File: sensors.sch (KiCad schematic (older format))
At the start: 1 part, among them U5 ICM-20948

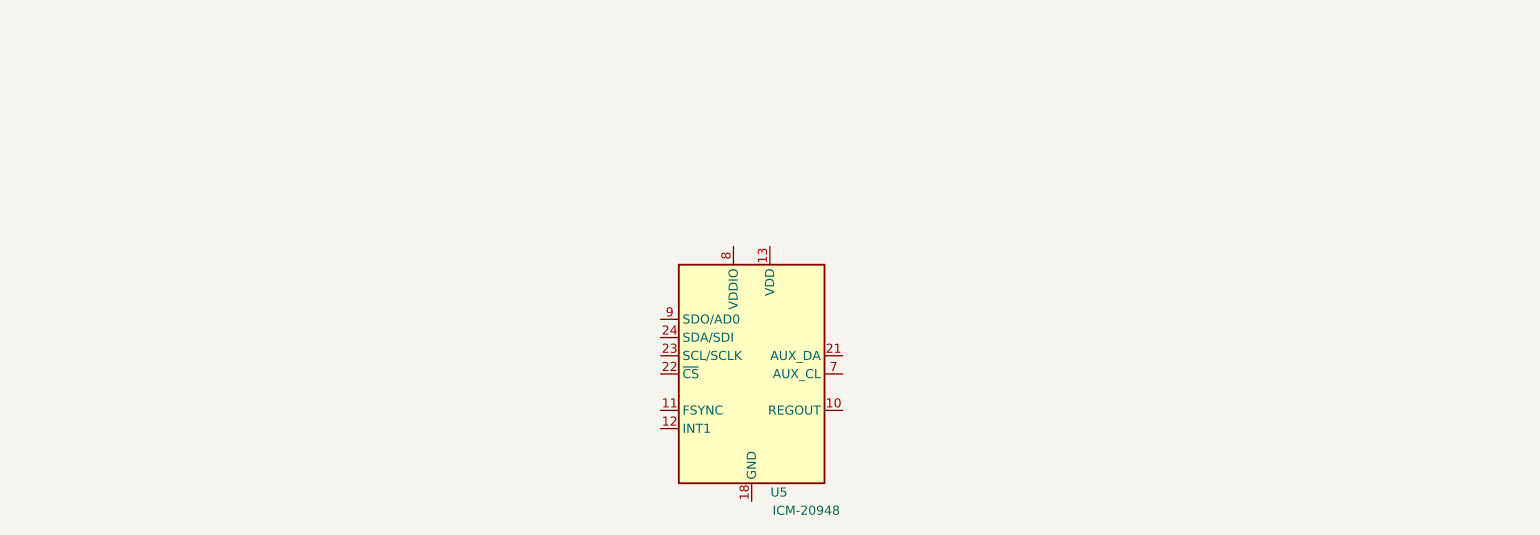
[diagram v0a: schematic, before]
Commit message: First full version of a schematic
This commit is a quicksave of completed but not reviewed schematic.
Added pressure sensor, finished IMU wiring, finished top-level
schematic, added pin header, placed LEDs and many others.
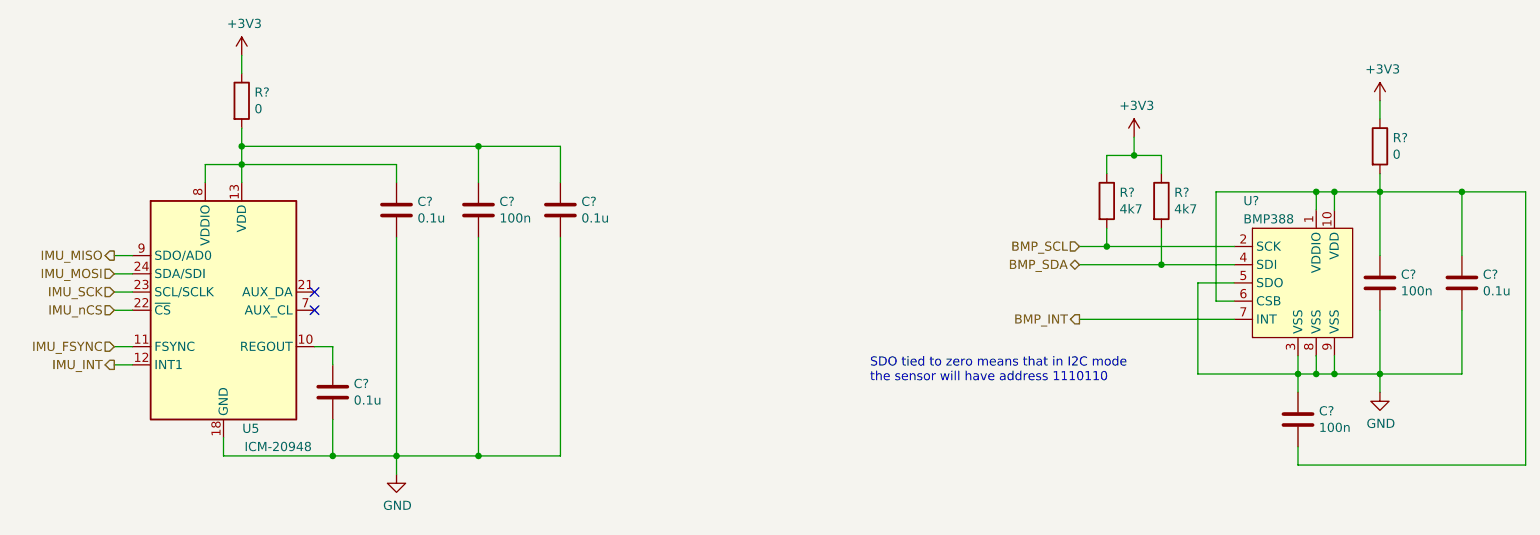
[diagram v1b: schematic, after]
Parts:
- added C? (x3): 100n, symbol Device:C
- added C? (x4): 0.1u, symbol Device:C
- added R? (x2): 4k7, symbol Device:R
- added R? (x2): 0, symbol Device:R
- added U?: BMP388, himudev:Bosch_LGA-10_2x2mm_P0.5mm, symbol himudev:BMP388
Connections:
- net at U5.10 (REGOUT): now also C?.1
- net IMU_FSYNC: now reaches U5.11 (FSYNC)
- net IMU_INT: now reaches U5.12 (INT1)
- net at U5.13 (VDD): now also U5.8 (VDDIO), C?.1, C?.1, C?.1, R?.2
- net GND: now reaches U5.18 (GND), U5.20 (GND)
- net GND: now also C?.1, C?.2, C?.2, C?.2, C?.2, C?.2, C?.2, U?.3 (VSS), U?.5 (SDO), U?.8 (VSS), U?.9 (VSS)
- net IMU_nCS: now reaches U5.22 (~CS)
- net IMU_SCK: now reaches U5.23 (SCL/SCLK)
- net IMU_MOSI: now reaches U5.24 (SDA/SDI)
- net IMU_MISO: now reaches U5.9 (SDO/AD0)
- new net: C?.1, C?.1, C?.2, R?.2, U?.1 (VDDIO), U?.10 (VDD), U?.6 (CSB)
- new net +3V3: R?.1, R?.1, R?.1, R?.1
- new net BMP_INT: U?.7 (INT)
- new net BMP_SCL: R?.2, U?.2 (SCK)
- new net BMP_SDA: R?.2, U?.4 (SDI)
- no-connect marks 0 -> 2
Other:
- note added: "SDO tied to zero means that in I2C mode\nthe sensor will have address 1110110"
- moved on the sheet: U5

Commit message: Add ERC fixes, mostly PWR_FLAGs
Also, fixed MCP1726 symbol.
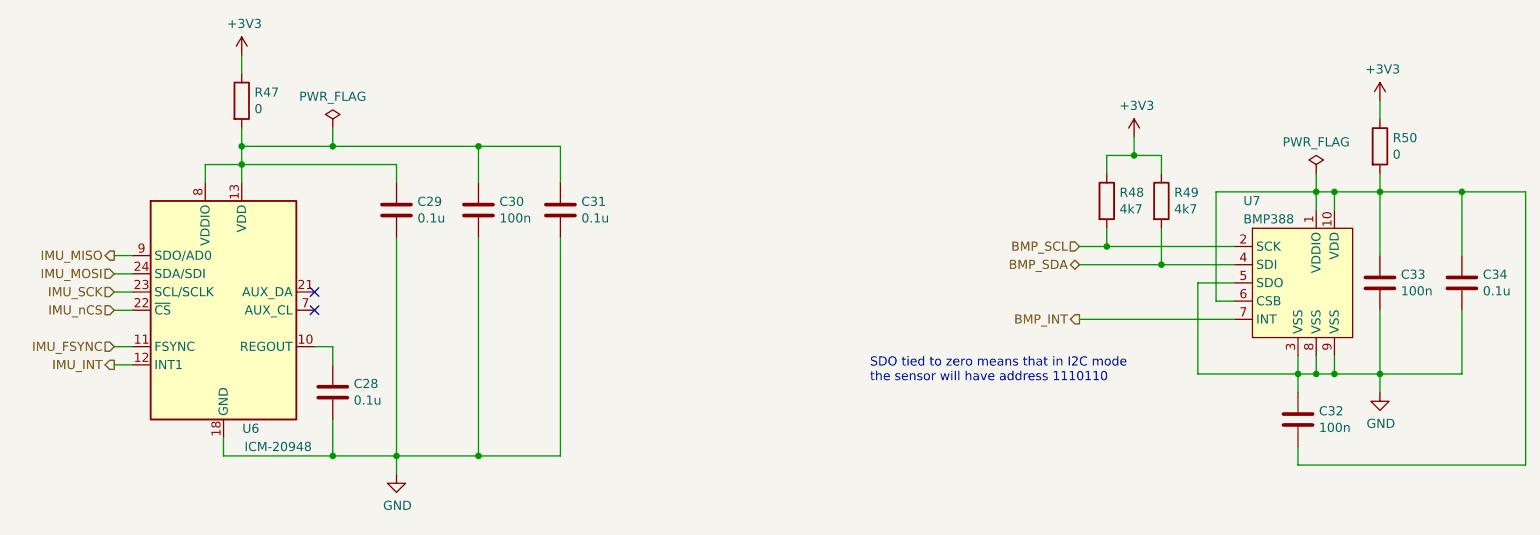
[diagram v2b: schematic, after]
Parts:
- gave numbers to parts that had none: 12
- renumbered U5 to U6
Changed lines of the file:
@@
 P 2750 3650
 AR Path="/5E167171" Ref="U?"  Part="1"
-AR Path="/5E166146/5E167171" Ref="U5"  Part="1"
-F 0 "U5" H 2900 3000 50  0000 C CNN
+AR Path="/5E166146/5E167171" Ref="U6"  Part="1"
+F 0 "U6" H 2900 3000 50  0000 C CNN
 F 1 "ICM-20948" H 3050 2900 50  0000 C CNN
 F 2 "Sensor_Motion:InvenSense_QFN-24_3x3mm_P0.4mm" H 2750 2650 50  0001 C CNN
@@
 $EndComp
 $Comp
-L himudev:BMP388 U?
+L himudev:BMP388 U7
 U 1 1 5E4A2210
 P 8650 3500
-F 0 "U?" H 8350 3950 50  0000 L CNN
+F 0 "U7" H 8350 3950 50  0000 L CNN
 F 1 "BMP388" H 8350 3850 50  0000 L CNN
 F 2 "himudev:Bosch_LGA-10_2x2mm_P0.5mm" H 8700 2750 50  0001 C CNN
@@
 $EndComp
 $Comp
-L Device:C C?
+L Device:C C32
 U 1 1 5E4A42CC
 P 8650 4250
-F 0 "C?" H 8765 4296 50  0000 L CNN
+F 0 "C32" H 8765 4296 50  0000 L CNN
 F 1 "100n" H 8765 4205 50  0000 L CNN
 F 2 "" H 8688 4100 50  0001 C CNN
@@
 $EndComp
 $Comp
-L Device:C C?
+L Device:C C33
 U 1 1 5E4A48E4
 P 9100 3500
-F 0 "C?" H 9215 3546 50  0000 L CNN
+F 0 "C33" H 9215 3546 50  0000 L CNN
 F 1 "100n" H 9215 3455 50  0000 L CNN
 F 2 "" H 9138 3350 50  0001 C CNN
@@
 $EndComp
 $Comp
-L Device:R R?
+L Device:R R49
 U 1 1 5E4A4DD8
 P 7900 3050
-F 0 "R?" H 7970 3096 50  0000 L CNN
+F 0 "R49" H 7970 3096 50  0000 L CNN
 F 1 "4k7" H 7970 3005 50  0000 L CNN
 F 2 "" V 7830 3050 50  0001 C CNN
@@
 $EndComp
 $Comp
-L Device:R R?
+L Device:R R48
 U 1 1 5E4A517E
 P 7600 3050
-F 0 "R?" H 7670 3096 50  0000 L CNN
+F 0 "R48" H 7670 3096 50  0000 L CNN
 F 1 "4k7" H 7670 3005 50  0000 L CNN
 F 2 "" V 7530 3050 50  0001 C CNN
@@
 	7900 3400 7900 3200
 $Comp
-L power:+3V3 #PWR?
+L power:+3V3 #PWR061
 U 1 1 5E4A8209
 P 7750 2700
-F 0 "#PWR?" H 7750 2550 50  0001 C CNN
+F 0 "#PWR061" H 7750 2550 50  0001 C CNN
 F 1 "+3V3" H 7765 2873 50  0000 C CNN
 F 2 "" H 7750 2700 50  0001 C CNN
@@
 Connection ~ 8650 4000
 $Comp
-L power:GND #PWR?
+L power:GND #PWR063
 U 1 1 5E4AE342
 P 9100 4100
-F 0 "#PWR?" H 9100 3850 50  0001 C CNN
+F 0 "#PWR063" H 9100 3850 50  0001 C CNN
 F 1 "GND" H 9105 3927 50  0000 C CNN
 F 2 "" H 9100 4100 50  0001 C CNN
@@
 Connection ~ 8850 3000
 $Comp
-L Device:C C?
+L Device:C C34
 U 1 1 5E4B2601
 P 9550 3500
-F 0 "C?" H 9665 3546 50  0000 L CNN
+F 0 "C34" H 9665 3546 50  0000 L CNN
 F 1 "0.1u" H 9665 3455 50  0000 L CNN
 F 2 "" H 9588 3350 50  0001 C CNN
@@
 Connection ~ 9100 4000
 $Comp
-L power:+3V3 #PWR?
+L power:+3V3 #PWR062
 U 1 1 5E4B6048
 P 9100 2500
-F 0 "#PWR?" H 9100 2350 50  0001 C CNN
+F 0 "#PWR062" H 9100 2350 50  0001 C CNN
 F 1 "+3V3" H 9115 2673 50  0000 C CNN
 F 2 "" H 9100 2500 50  0001 C CNN
@@
 	9100 4000 9100 4100
 $Comp
-L Device:R R?
+L Device:R R50
 U 1 1 5EC5840F
 P 9100 2750
-F 0 "R?" H 9170 2796 50  0000 L CNN
+F 0 "R50" H 9170 2796 50  0000 L CNN
 F 1 "0" H 9170 2705 50  0000 L CNN
 F 2 "" V 9030 2750 50  0001 C CNN
@@
 	9100 2500 9100 2600
 $Comp
-L Device:C C?
+L Device:C C30
 U 1 1 5EC5B4FF
 P 4150 3100
-F 0 "C?" H 4265 3146 50  0000 L CNN
+F 0 "C30" H 4265 3146 50  0000 L CNN
 F 1 "100n" H 4265 3055 50  0000 L CNN
 F 2 "" H 4188 2950 50  0001 C CNN
@@
 $EndComp
 $Comp
-L Device:C C?
+L Device:C C31
 U 1 1 5EC5B505
 P 4600 3100
-F 0 "C?" H 4715 3146 50  0000 L CNN
+F 0 "C31" H 4715 3146 50  0000 L CNN
 F 1 "0.1u" H 4715 3055 50  0000 L CNN
 F 2 "" H 4638 2950 50  0001 C CNN
@@
 $EndComp
 $Comp
-L power:GND #PWR?
+L power:GND #PWR060
 U 1 1 5EC5DA97
 P 3700 4550
-F 0 "#PWR?" H 3700 4300 50  0001 C CNN
+F 0 "#PWR060" H 3700 4300 50  0001 C CNN
 F 1 "GND" H 3705 4377 50  0000 C CNN
 F 2 "" H 3700 4550 50  0001 C CNN
@@
 $EndComp
 $Comp
-L Device:C C?
+L Device:C C29
 U 1 1 5EC5DEA9
 P 3700 3100
-F 0 "C?" H 3815 3146 50  0000 L CNN
+F 0 "C29" H 3815 3146 50  0000 L CNN
 F 1 "0.1u" H 3815 3055 50  0000 L CNN
 F 2 "" H 3738 2950 50  0001 C CNN
@@
 $EndComp
 $Comp
-L Device:C C?
+L Device:C C28
 U 1 1 5EC5E315
 P 3350 4100
-F 0 "C?" H 3465 4146 50  0000 L CNN
+F 0 "C28" H 3465 4146 50  0000 L CNN
 F 1 "0.1u" H 3465 4055 50  0000 L CNN
 F 2 "" H 3388 3950 50  0001 C CNN
@@
 	2850 2950 2850 2850
 Wire Wire Line
-	2850 2750 4150 2750
+	2850 2750 3350 2750
 Wire Wire Line
 	4600 2750 4600 2950
@@
 IMU_nCS
 $Comp
-L power:+3V3 #PWR?
+L power:+3V3 #PWR059
 U 1 1 5EC713A1
 P 2850 2250
-F 0 "#PWR?" H 2850 2100 50  0001 C CNN
+F 0 "#PWR059" H 2850 2100 50  0001 C CNN
 F 1 "+3V3" H 2865 2423 50  0000 C CNN
 F 2 "" H 2850 2250 50  0001 C CNN
@@
 $EndComp
 $Comp
-L Device:R R?
+L Device:R R47
 U 1 1 5EC713A7
 P 2850 2500
-F 0 "R?" H 2920 2546 50  0000 L CNN
+F 0 "R47" H 2920 2546 50  0000 L CNN
 F 1 "0" H 2920 2455 50  0000 L CNN
 F 2 "" V 2780 2500 50  0001 C CNN
@@
 Wire Wire Line
 	2150 3650 2250 3650
+$Comp
+L power:PWR_FLAG #FLG0106
+U 1 1 5E3AD934
+P 8750 2900
+F 0 "#FLG0106" H 8750 2975 50  0001 C CNN
+F 1 "PWR_FLAG" H 8750 3073 50  0000 C CNN
+F 2 "" H 8750 2900 50  0001 C CNN
+F 3 "~" H 8750 2900 50  0001 C CNN
+	1    8750 2900
+	1    0    0    -1
+$EndComp
+Wire Wire Line
+	8750 2900 8750 3000
+$Comp
+L power:PWR_FLAG #FLG0107
+U 1 1 5E3AF8FB
+P 3350 2650
+F 0 "#FLG0107" H 3350 2725 50  0001 C CNN
+F 1 "PWR_FLAG" H 3350 2823 50  0000 C CNN
+F 2 "" H 3350 2650 50  0001 C CNN
+F 3 "~" H 3350 2650 50  0001 C CNN
+	1    3350 2650
+	1    0    0    -1
+$EndComp
+Wire Wire Line
+	3350 2650 3350 2750
+Connection ~ 3350 2750
+Wire Wire Line
+	3350 2750 4150 2750
 $EndSCHEMATC

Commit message: Assigned footprints, generated netlist
I can already see some footprints issues. Eg. the switches have to be
changed to the SMT version. There are some silkscreen issues in custom
oscillator footprints. Otherwise looks promising :)
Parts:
- C28, C29, C30, C31, C32, C33, C34: footprint (none) -> Capacitor_SMD:C_0805_2012Metric_Pad1.15x1.40mm_HandSolder
- R47, R48, R49, R50: footprint (none) -> Resistor_SMD:R_0805_2012Metric_Pad1.15x1.40mm_HandSolder
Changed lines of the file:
@@
 F 0 "C32" H 8765 4296 50  0000 L CNN
 F 1 "100n" H 8765 4205 50  0000 L CNN
-F 2 "" H 8688 4100 50  0001 C CNN
+F 2 "Capacitor_SMD:C_0805_2012Metric_Pad1.15x1.40mm_HandSolder" H 8688 4100 50  0001 C CNN
 F 3 "~" H 8650 4250 50  0001 C CNN
 	1    8650 4250
@@
 F 0 "C33" H 9215 3546 50  0000 L CNN
 F 1 "100n" H 9215 3455 50  0000 L CNN
-F 2 "" H 9138 3350 50  0001 C CNN
+F 2 "Capacitor_SMD:C_0805_2012Metric_Pad1.15x1.40mm_HandSolder" H 9138 3350 50  0001 C CNN
 F 3 "~" H 9100 3500 50  0001 C CNN
 	1    9100 3500
@@
 F 0 "R49" H 7970 3096 50  0000 L CNN
 F 1 "4k7" H 7970 3005 50  0000 L CNN
-F 2 "" V 7830 3050 50  0001 C CNN
+F 2 "Resistor_SMD:R_0805_2012Metric_Pad1.15x1.40mm_HandSolder" V 7830 3050 50  0001 C CNN
 F 3 "~" H 7900 3050 50  0001 C CNN
 	1    7900 3050
@@
 F 0 "R48" H 7670 3096 50  0000 L CNN
 F 1 "4k7" H 7670 3005 50  0000 L CNN
-F 2 "" V 7530 3050 50  0001 C CNN
+F 2 "Resistor_SMD:R_0805_2012Metric_Pad1.15x1.40mm_HandSolder" V 7530 3050 50  0001 C CNN
 F 3 "~" H 7600 3050 50  0001 C CNN
 	1    7600 3050
@@
 F 0 "C34" H 9665 3546 50  0000 L CNN
 F 1 "0.1u" H 9665 3455 50  0000 L CNN
-F 2 "" H 9588 3350 50  0001 C CNN
+F 2 "Capacitor_SMD:C_0805_2012Metric_Pad1.15x1.40mm_HandSolder" H 9588 3350 50  0001 C CNN
 F 3 "~" H 9550 3500 50  0001 C CNN
 	1    9550 3500
@@
 F 0 "R50" H 9170 2796 50  0000 L CNN
 F 1 "0" H 9170 2705 50  0000 L CNN
-F 2 "" V 9030 2750 50  0001 C CNN
+F 2 "Resistor_SMD:R_0805_2012Metric_Pad1.15x1.40mm_HandSolder" V 9030 2750 50  0001 C CNN
 F 3 "~" H 9100 2750 50  0001 C CNN
 	1    9100 2750
@@
 F 0 "C30" H 4265 3146 50  0000 L CNN
 F 1 "100n" H 4265 3055 50  0000 L CNN
-F 2 "" H 4188 2950 50  0001 C CNN
+F 2 "Capacitor_SMD:C_0805_2012Metric_Pad1.15x1.40mm_HandSolder" H 4188 2950 50  0001 C CNN
 F 3 "~" H 4150 3100 50  0001 C CNN
 	1    4150 3100
@@
 F 0 "C31" H 4715 3146 50  0000 L CNN
 F 1 "0.1u" H 4715 3055 50  0000 L CNN
-F 2 "" H 4638 2950 50  0001 C CNN
+F 2 "Capacitor_SMD:C_0805_2012Metric_Pad1.15x1.40mm_HandSolder" H 4638 2950 50  0001 C CNN
 F 3 "~" H 4600 3100 50  0001 C CNN
 	1    4600 3100
@@
 F 0 "C29" H 3815 3146 50  0000 L CNN
 F 1 "0.1u" H 3815 3055 50  0000 L CNN
-F 2 "" H 3738 2950 50  0001 C CNN
+F 2 "Capacitor_SMD:C_0805_2012Metric_Pad1.15x1.40mm_HandSolder" H 3738 2950 50  0001 C CNN
 F 3 "~" H 3700 3100 50  0001 C CNN
 	1    3700 3100
@@
 F 0 "C28" H 3465 4146 50  0000 L CNN
 F 1 "0.1u" H 3465 4055 50  0000 L CNN
-F 2 "" H 3388 3950 50  0001 C CNN
+F 2 "Capacitor_SMD:C_0805_2012Metric_Pad1.15x1.40mm_HandSolder" H 3388 3950 50  0001 C CNN
 F 3 "~" H 3350 4100 50  0001 C CNN
 	1    3350 4100
@@
 F 0 "R47" H 2920 2546 50  0000 L CNN
 F 1 "0" H 2920 2455 50  0000 L CNN
-F 2 "" V 2780 2500 50  0001 C CNN
+F 2 "Resistor_SMD:R_0805_2012Metric_Pad1.15x1.40mm_HandSolder" V 2780 2500 50  0001 C CNN
 F 3 "~" H 2850 2500 50  0001 C CNN
 	1    2850 2500

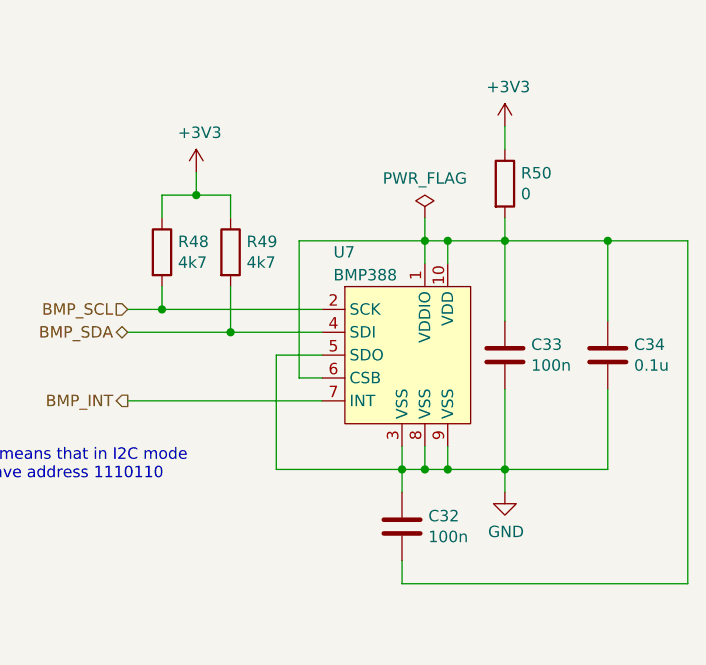
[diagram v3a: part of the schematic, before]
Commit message: Placed pressure sensor, connector changed to USB-C
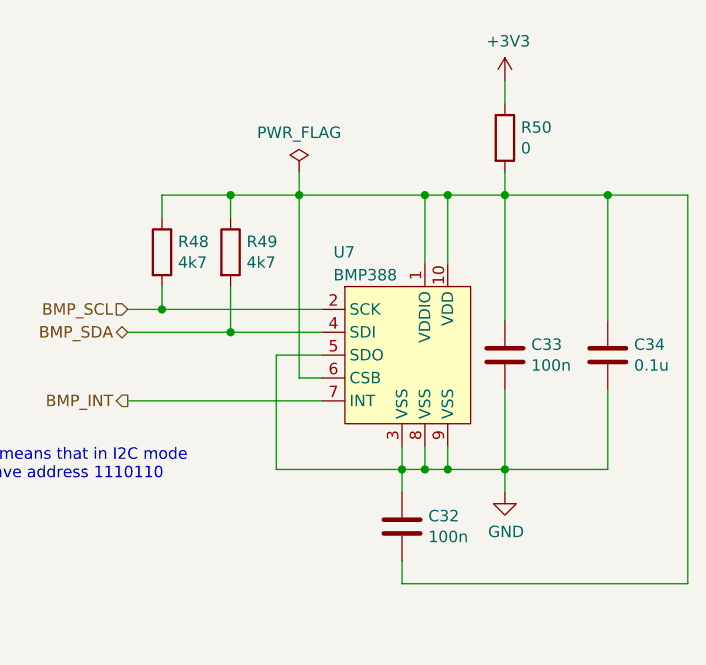
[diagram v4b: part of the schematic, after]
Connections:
- net +3V3: no longer R48.1, R49.1
- net at C32.2, C33.1, C34.1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: now also R48.1, R49.1
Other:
- moved on the sheet: R50
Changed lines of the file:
@@
 Wire Wire Line
 	7900 3400 7900 3200
-$Comp
-L power:+3V3 #PWR061
-U 1 1 5E4A8209
-P 7750 2700
-F 0 "#PWR061" H 7750 2550 50  0001 C CNN
-F 1 "+3V3" H 7765 2873 50  0000 C CNN
-F 2 "" H 7750 2700 50  0001 C CNN
-F 3 "" H 7750 2700 50  0001 C CNN
-	1    7750 2700
-	1    0    0    -1
-$EndComp
 Wire Wire Line
 	7900 2900 7900 2800
 Wire Wire Line
-	7900 2800 7750 2800
-Wire Wire Line
 	7600 2800 7600 2900
-Wire Wire Line
-	7750 2700 7750 2800
-Connection ~ 7750 2800
-Wire Wire Line
-	7750 2800 7600 2800
 Text Notes 6300 4050 0    50   ~ 0
 SDO tied to zero means that in I2C mode\nthe sensor will have address 1110110
@@
 	8300 3600 8200 3600
 Wire Wire Line
-	8200 3000 8750 3000
-Wire Wire Line
-	8750 3000 8750 3100
-Wire Wire Line
 	8100 3500 8300 3500
-Wire Wire Line
-	8200 3000 8200 3600
 Wire Wire Line
 	8100 4000 8650 4000
@@
 Wire Wire Line
 	7450 3700 8300 3700
-Wire Wire Line
-	8850 3100 8850 3000
-Wire Wire Line
-	8850 3000 8750 3000
-Connection ~ 8750 3000
-Wire Wire Line
-	9100 3350 9100 3000
-Wire Wire Line
-	9100 3000 8850 3000
-Connection ~ 8850 3000
 $Comp
 L Device:C C34
@@
 $EndComp
 Wire Wire Line
-	9550 3350 9550 3000
-Wire Wire Line
-	9550 3000 9100 3000
-Connection ~ 9100 3000
-Wire Wire Line
 	8850 4000 9100 4000
 Wire Wire Line
@@
 L power:+3V3 #PWR062
 U 1 1 5E4B6048
-P 9100 2500
-F 0 "#PWR062" H 9100 2350 50  0001 C CNN
-F 1 "+3V3" H 9115 2673 50  0000 C CNN
-F 2 "" H 9100 2500 50  0001 C CNN
-F 3 "" H 9100 2500 50  0001 C CNN
-	1    9100 2500
-	1    0    0    -1
-$EndComp
-Wire Wire Line
-	9100 2900 9100 3000
+P 9100 2300
+F 0 "#PWR062" H 9100 2150 50  0001 C CNN
+F 1 "+3V3" H 9115 2473 50  0000 C CNN
+F 2 "" H 9100 2300 50  0001 C CNN
+F 3 "" H 9100 2300 50  0001 C CNN
+	1    9100 2300
+	1    0    0    -1
+$EndComp
 Text HLabel 7450 3300 0    50   Input ~ 0
 BMP_SCL
@@
 	8650 4500 9900 4500
 Wire Wire Line
-	9900 4500 9900 3000
-Wire Wire Line
-	9900 3000 9550 3000
-Wire Wire Line
 	8650 4400 8650 4500
-Connection ~ 9550 3000
 Wire Wire Line
 	9100 4000 9100 4100
@@
 L Device:R R50
 U 1 1 5EC5840F
-P 9100 2750
-F 0 "R50" H 9170 2796 50  0000 L CNN
-F 1 "0" H 9170 2705 50  0000 L CNN
-F 2 "Resistor_SMD:R_0805_2012Metric_Pad1.15x1.40mm_HandSolder" V 9030 2750 50  0001 C CNN
-F 3 "~" H 9100 2750 50  0001 C CNN
-	1    9100 2750
-	1    0    0    -1
-$EndComp
-Wire Wire Line
-	9100 2500 9100 2600
+P 9100 2550
+F 0 "R50" H 9170 2596 50  0000 L CNN
+F 1 "0" H 9170 2505 50  0000 L CNN
+F 2 "Resistor_SMD:R_0805_2012Metric_Pad1.15x1.40mm_HandSolder" V 9030 2550 50  0001 C CNN
+F 3 "~" H 9100 2550 50  0001 C CNN
+	1    9100 2550
+	1    0    0    -1
+$EndComp
+Wire Wire Line
+	9100 2300 9100 2400
 $Comp
 L Device:C C30
@@
 L power:PWR_FLAG #FLG0106
 U 1 1 5E3AD934
-P 8750 2900
-F 0 "#FLG0106" H 8750 2975 50  0001 C CNN
-F 1 "PWR_FLAG" H 8750 3073 50  0000 C CNN
-F 2 "" H 8750 2900 50  0001 C CNN
-F 3 "~" H 8750 2900 50  0001 C CNN
-	1    8750 2900
-	1    0    0    -1
-$EndComp
-Wire Wire Line
-	8750 2900 8750 3000
+P 8200 2700
+F 0 "#FLG0106" H 8200 2775 50  0001 C CNN
+F 1 "PWR_FLAG" H 8200 2873 50  0000 C CNN
+F 2 "" H 8200 2700 50  0001 C CNN
+F 3 "~" H 8200 2700 50  0001 C CNN
+	1    8200 2700
+	1    0    0    -1
+$EndComp
 $Comp
 L power:PWR_FLAG #FLG0107
@@
 Wire Wire Line
 	3350 2750 4150 2750
+Wire Wire Line
+	7600 2800 7900 2800
+Wire Wire Line
+	7900 2800 8200 2800
+Connection ~ 7900 2800
+Connection ~ 9550 2800
+Connection ~ 9100 2800
+Wire Wire Line
+	9100 2800 9550 2800
+Connection ~ 8200 2800
+Wire Wire Line
+	8200 2800 8750 2800
+Wire Wire Line
+	8200 2800 8200 3600
+Wire Wire Line
+	9100 2800 9100 3350
+Wire Wire Line
+	8850 2800 8850 3100
+Connection ~ 8850 2800
+Wire Wire Line
+	8850 2800 9100 2800
+Wire Wire Line
+	8750 2800 8750 3100
+Connection ~ 8750 2800
+Wire Wire Line
+	8750 2800 8850 2800
+Wire Wire Line
+	9550 2800 9900 2800
+Wire Wire Line
+	9900 2800 9900 4500
+Wire Wire Line
+	9550 2800 9550 3350
+Wire Wire Line
+	9100 2700 9100 2800
+Wire Wire Line
+	8200 2700 8200 2800
 $EndSCHEMATC
